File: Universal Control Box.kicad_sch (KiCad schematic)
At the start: 26 parts, among them J101 Conn_01x06, J102 Conn_01x07, J103 USB_C_Receptacle_USB2.0, U101 ESP32-WROOM-32, U102 PCF8575DBR (PCF1), U103 XC6220B331MR-G

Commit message: Some improvements & added labeling
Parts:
- D101: footprint LED_SMD:LED_0603_1608Metric -> LED_SMD:LED_0805_2012Metric; LCSC C2286 -> C84256
- D102: footprint LED_SMD:LED_0603_1608Metric -> LED_SMD:LED_0805_2012Metric; LCSC C72043 -> C2297
- D103: footprint LED_SMD:LED_0603_1608Metric -> LED_SMD:LED_0805_2012Metric; LCSC C2286 -> C2296
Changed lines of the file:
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@@
 	(title_block
 		(title "Universal Control Box")
-		(date "2023-12-28")
 		(rev "v1.0")
 	)
@@
 			)
 		)
-		(property "Footprint" "LED_SMD:LED_0603_1608Metric"
+		(property "Footprint" "LED_SMD:LED_0805_2012Metric"
 			(at 29.21 143.51 0)
 			(effects
@@
 			)
 		)
-		(property "LCSC" "C72043"
+		(property "LCSC" "C2297"
 			(at 29.21 143.51 0)
 			(effects
@@
 			)
 		)
-		(property "Footprint" "LED_SMD:LED_0603_1608Metric"
+		(property "Footprint" "LED_SMD:LED_0805_2012Metric"
 			(at 40.64 143.51 0)
 			(effects
@@
 			)
 		)
-		(property "LCSC" "C2286"
+		(property "LCSC" "C2296"
 			(at 40.64 143.51 0)
 			(effects
@@
 			)
 		)
-		(property "Footprint" "LED_SMD:LED_0603_1608Metric"
+		(property "Footprint" "LED_SMD:LED_0805_2012Metric"
 			(at 19.05 143.51 0)
 			(effects
@@
 			)
 		)
-		(property "LCSC" "C2286"
+		(property "LCSC" "C84256"
 			(at 19.05 143.51 0)
 			(effects

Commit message: Included symbols/footprints/3dmodels to repo
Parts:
- F101: footprint Adam_Custom_Footprints:Fuse_1812_4532Metric -> footprints:Fuse_1812_4532Metric
- J102: footprint Adam_Custom_Footprints:PinSocket_1x07_P2.54mm_Vertical_SSD1309 -> footprints:PinSocket_1x07_P2.54mm_Vertical_SSD1309
- J103: footprint Josh_Custom_Footprints:USB_C_Receptable_918-418K2023S40001 -> footprints:USB_C_Receptable_918-418K2023S40001
- U101: footprint Josh_Custom_Footprints:ESP32-WROOM-32 -> footprints:ESP32-WROOM-32
- U102: footprint Adam_Custom_Footprints:TexasInstruments_PCF8575DBR -> footprints:TexasInstruments_PCF8575DBR
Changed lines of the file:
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@@
 			)
 		)
-		(property "Footprint" "Josh_Custom_Footprints:USB_C_Receptable_918-418K2023S40001"
+		(property "Footprint" "footprints:USB_C_Receptable_918-418K2023S40001"
 			(at 121.92 128.27 0)
 			(effects
@@
 			)
 		)
-		(property "Footprint" "Adam_Custom_Footprints:PinSocket_1x07_P2.54mm_Vertical_SSD1309"
+		(property "Footprint" "footprints:PinSocket_1x07_P2.54mm_Vertical_SSD1309"
 			(at 62.23 179.07 0)
 			(effects
@@
 			)
 		)
-		(property "Footprint" "Adam_Custom_Footprints:TexasInstruments_PCF8575DBR"
+		(property "Footprint" "footprints:TexasInstruments_PCF8575DBR"
 			(at 128.27 26.67 0)
 			(effects
@@
 			)
 		)
-		(property "Footprint" "Adam_Custom_Footprints:Fuse_1812_4532Metric"
+		(property "Footprint" "footprints:Fuse_1812_4532Metric"
 			(at 147.32 111.76 0)
 			(effects
@@
 			)
 		)
-		(property "Footprint" "Josh_Custom_Footprints:ESP32-WROOM-32"
+		(property "Footprint" "footprints:ESP32-WROOM-32"
 			(at 46.99 116.84 0)
 			(effects

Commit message: update design
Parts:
- added U104: 74AHCT1G125, Package_TO_SOT_SMD:SOT-23-5, symbol 74xGxx:74AHCT1G125
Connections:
- net +5V: now also U104.5 (VCC)
- net GND: now also U104.1, U104.3 (GND)
- net LED_DATA: now also U104.2
- new net LED_DATA_OUT: U104.4
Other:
- note added: "Level Shifter"

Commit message: Fixes
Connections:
- net OLED_CS: now also U101.6 (IO34); no longer U101.29 (IO5)
- net OLED_DC: now also U101.7 (IO35); no longer U101.9 (IO33)
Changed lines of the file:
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@@
-	)
-	(no_connect
-		(at 62.23 104.14)
 	)
 	(no_connect
@@
 	)
 	(no_connect
+		(at 62.23 60.96)
+	)
+	(no_connect
+		(at 62.23 101.6)
+	)
+	(no_connect
 		(at 133.35 125.73)
 	)
@@
 	)
 	(no_connect
-		(at 62.23 106.68)
-	)
-	(no_connect
 		(at 62.23 53.34)
 	)
@@
 	(wire
 		(pts
-			(xy 62.23 60.96) (xy 74.93 60.96)
-		)
-		(stroke
-			(width 0)
-			(type default)
-		)
-	)
-	(wire
-		(pts
 			(xy 144.78 128.27) (xy 143.51 128.27)
 		)
@@
 	(wire
 		(pts
-			(xy 62.23 101.6) (xy 74.93 101.6)
-		)
-		(stroke
-			(width 0)
-			(type default)
-		)
-	)
-	(wire
-		(pts
 			(xy 62.23 55.88) (xy 74.93 55.88)
 		)
@@
 	(wire
 		(pts
+			(xy 62.23 104.14) (xy 74.93 104.14)
+		)
+		(stroke
+			(width 0)
+			(type default)
+		)
+	)
+	(wire
+		(pts
 			(xy 184.15 26.67) (xy 185.42 26.67)
 		)
@@
 		(pts
 			(xy 233.68 22.86) (xy 240.03 22.86)
+		)
+		(stroke
+			(width 0)
+			(type default)
+		)
+	)
+	(wire
+		(pts
+			(xy 62.23 106.68) (xy 74.93 106.68)
 		)
 		(stroke
@@
 	)
 	(label "OLED_CS"
+		(at 74.93 104.14 180)
+		(fields_autoplaced yes)
+		(effects
+			(font
+				(size 1.27 1.27)
+			)
+			(justify right bottom)
+		)
+	)
+	(label "OLED_CS"
 		(at 82.55 171.45 180)
 		(fields_autoplaced yes)
@@
 		)
 	)
+	(label "OLED_DC"
+		(at 74.93 106.68 180)
+		(fields_autoplaced yes)
+		(effects
+			(font
+				(size 1.27 1.27)
+			)
+			(justify right bottom)
+		)
+	)
 	(label "OLED_RESET"
 		(at 74.93 99.06 180)
@@
 		)
 	)
-	(label "OLED_DC"
-		(at 74.93 101.6 180)
-		(fields_autoplaced yes)
-		(effects
-			(font
-				(size 1.27 1.27)
-			)
-			(justify right bottom)
-		)
-	)
 	(label "I2C_SCL"
 		(at 74.93 86.36 180)
@@
 		(fields_autoplaced yes)
 		(effects
-			(font
-				(size 1.27 1.27)
-			)
-			(justify right bottom)
-		)
-	)
-	(label "OLED_CS"
-		(at 74.93 60.96 180)
-		(fields_autoplaced yes)
-		(effects

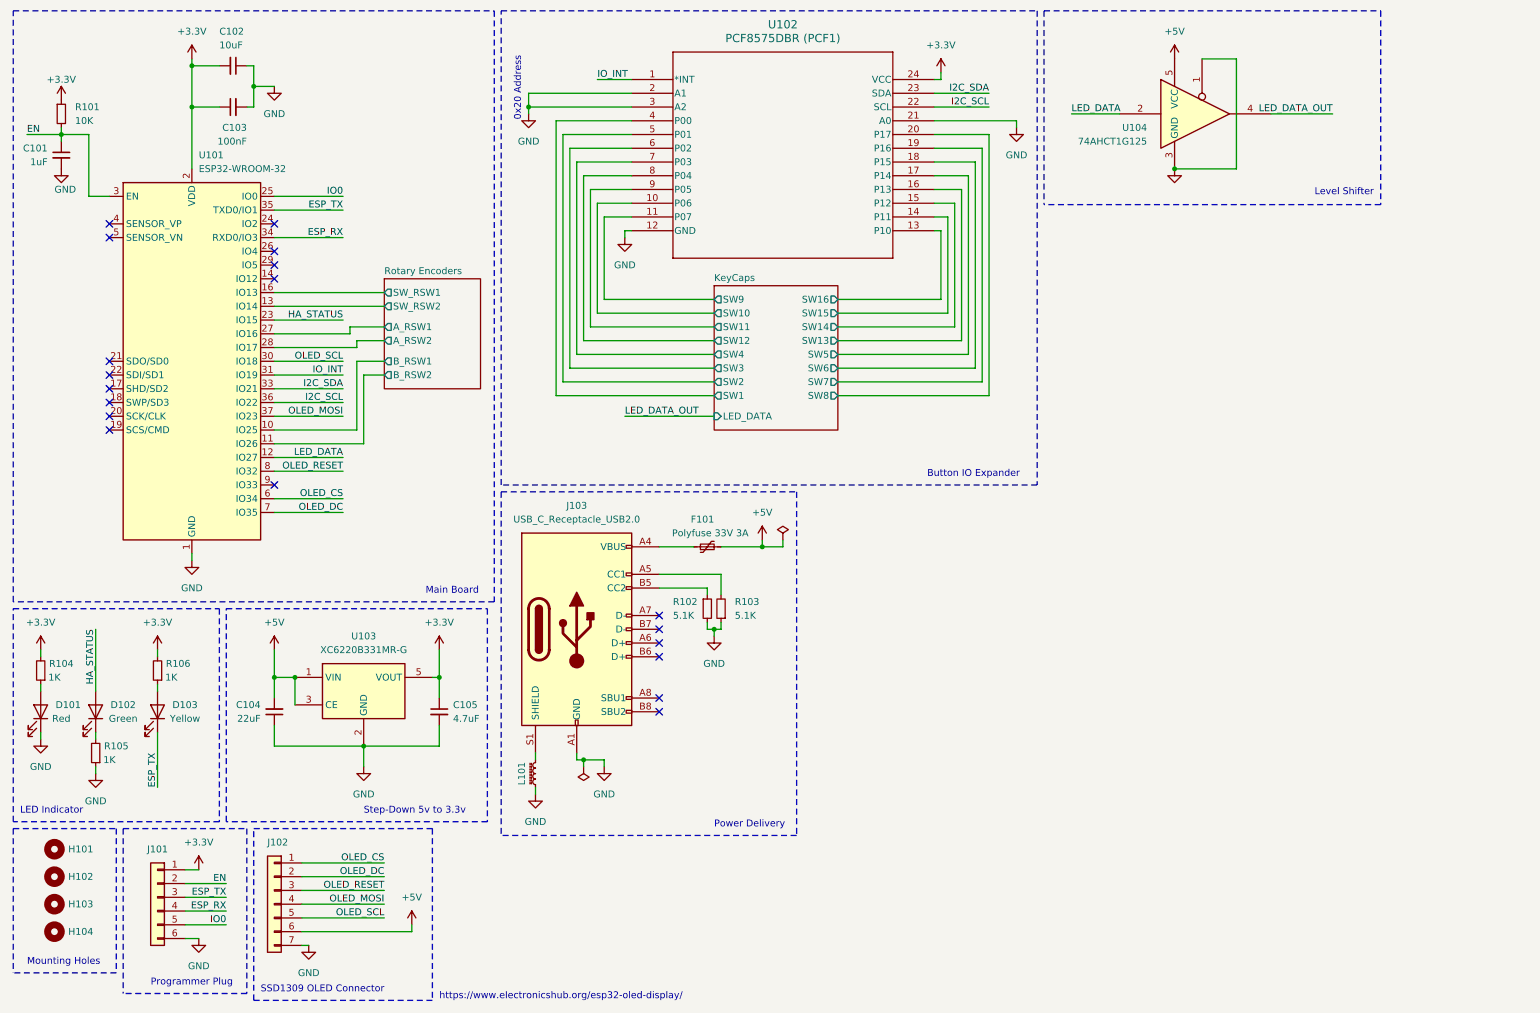
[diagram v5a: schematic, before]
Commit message: Fixed wiring for OLED display, push button for rotary & added chips for programming via USB C
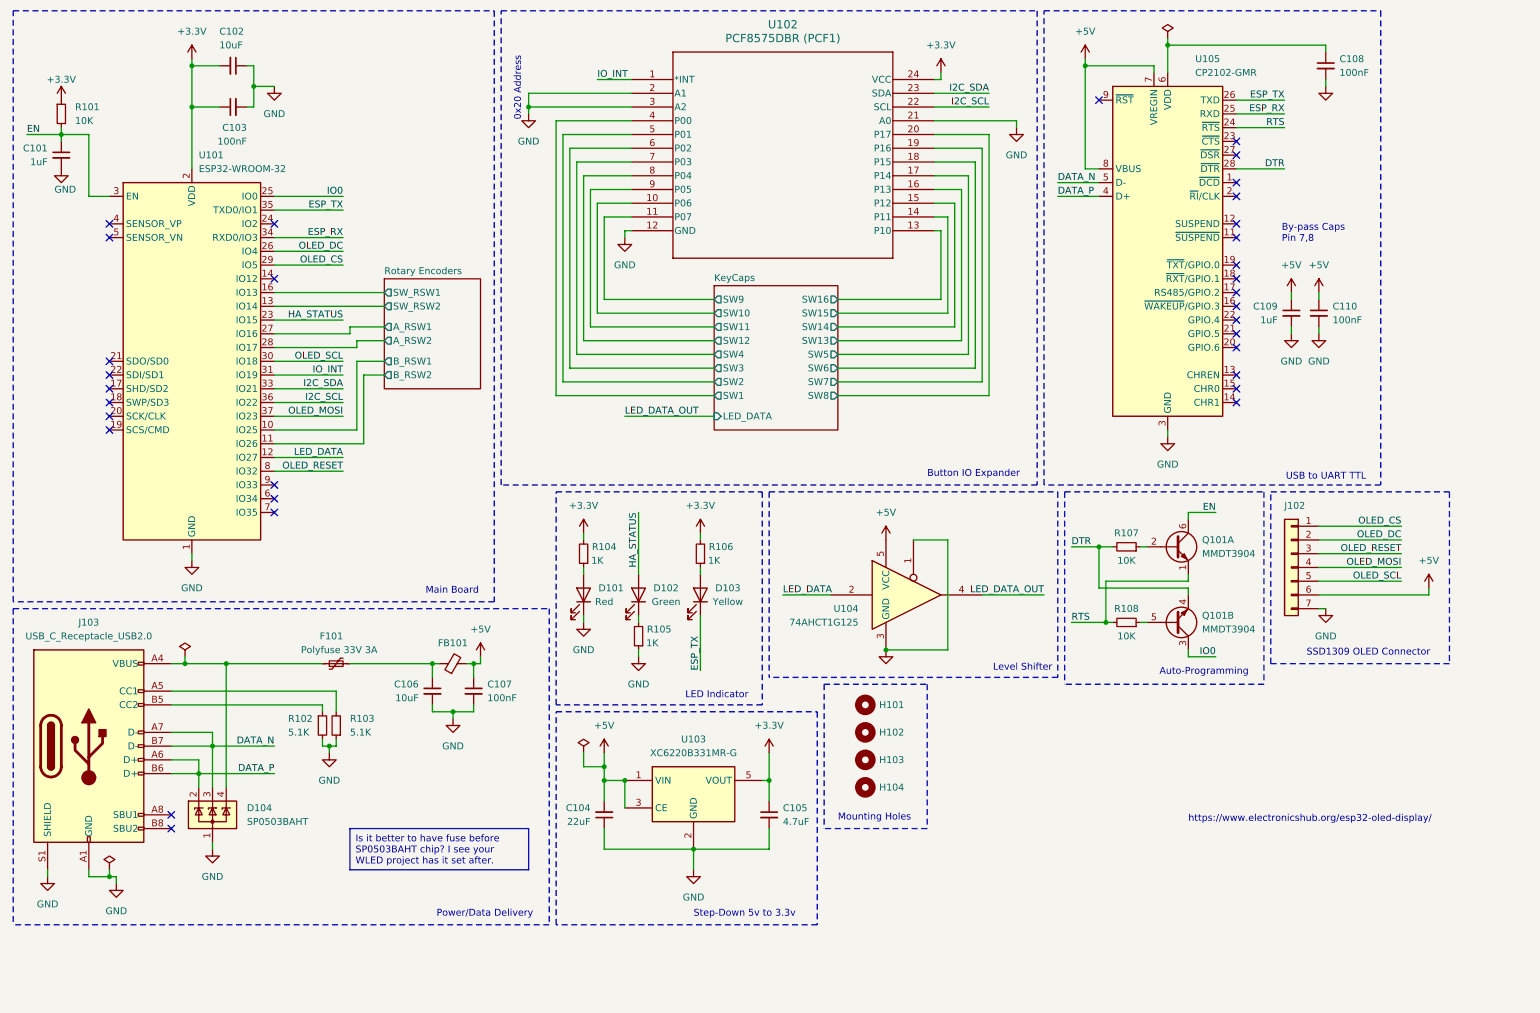
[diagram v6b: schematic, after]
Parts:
- removed J101: Conn_01x06, Connector_PinSocket_2.54mm:PinSocket_1x06_P2.54mm_Vertical, symbol Connector_Generic:Conn_01x06
- removed L101: L_Ferrite_Small, Inductor_SMD:L_0603_1608Metric, symbol Device:L_Ferrite_Small
- added C106: 10uF, Capacitor_SMD:C_0805_2012Metric, symbol Device:C_Small
- added C107, C108, C110: 100nF, Capacitor_SMD:C_0603_1608Metric, symbol Device:C_Small
- added C109: 1uF, Capacitor_SMD:C_0603_1608Metric, symbol Device:C_Small
- added D104: SP0503BAHT, Package_TO_SOT_SMD:SOT-143, symbol Power_Protection:SP0503BAHT
- added FB101: FerriteBead_Small, Resistor_SMD:R_0805_2012Metric, symbol Device:FerriteBead_Small
- added Q101: MMDT3904, Package_TO_SOT_SMD:SOT-363_SC-70-6, symbol Device:Q_Dual_NPN_NPN_E1B1C2E2B2C1
- added R107, R108: 10K, Resistor_SMD:R_0603_1608Metric, symbol Device:R_Small
- added U105: CP2102-GMR, Package_DFN_QFN:QFN-28-1EP_5x5mm_P0.5mm_EP3.35x3.35mm, symbol Interface_USB:CP2102N-Axx-xQFN28
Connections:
- net +5V: now also C107.1, C109.1, C110.1, FB101.2, U105.7 (VREGIN), U105.8 (VBUS); no longer F101.2
- net EN: now also Q101.6 (C1)
- net ESP_RX: now also U105.25 (RXD)
- net ESP_TX: now also U105.26 (TXD)
- net GND: now also J103.S1 (SHIELD), C106.2, C107.2, C108.2, C109.2, C110.2, D104.1 (A), U105.29 (GND), U105.3 (GND)
- net IO0: now also Q101.3 (C2)
- net OLED_CS: now also U101.29 (IO5); no longer U101.6 (IO34)
- net OLED_DC: now also U101.26 (IO4); no longer U101.7 (IO35)
- net at F101.1, J103.A4 (VBUS), J103.A9 (VBUS)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: now also D104.4 (K)
- net DATA_P: now reaches J103.A6 (D+)
- net DATA_P: now also J103.B6 (D+), D104.2 (K), U105.4 (D+)
- net DATA_N: now reaches J103.A7 (D-)
- net DATA_N: now also J103.B7 (D-), D104.3 (K), U105.5 (D-)
- new net: Q101.5 (B2), R108.1
- new net: C106.1, F101.2, FB101.1
- new net: C108.1, U105.6 (VDD)
- new net: Q101.2 (B1), R107.1
- new net DTR: Q101.4 (E2), R107.2, U105.28 (~{DTR})
- new net RTS: Q101.1 (E1), R108.2, U105.24 (~{RTS})
- no-connect marks 19 -> 32
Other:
- note added: "Auto-Programming"
- note added: "By-pass Caps Pin 7,8"
- note added: "Power/Data Delivery"
- note added: "USB to UART TTL"
- note removed: "Power Delivery"
- note removed: "Programmer Plug"
- moved on the sheet: C104, C105, D101, D102, D103, F101, H101, H102, H103, H104, J102, J103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
